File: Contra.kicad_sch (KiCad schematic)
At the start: 99 parts, among them J1 Conn_01x04, SW1 SW_PUSH, U1 ProMicro

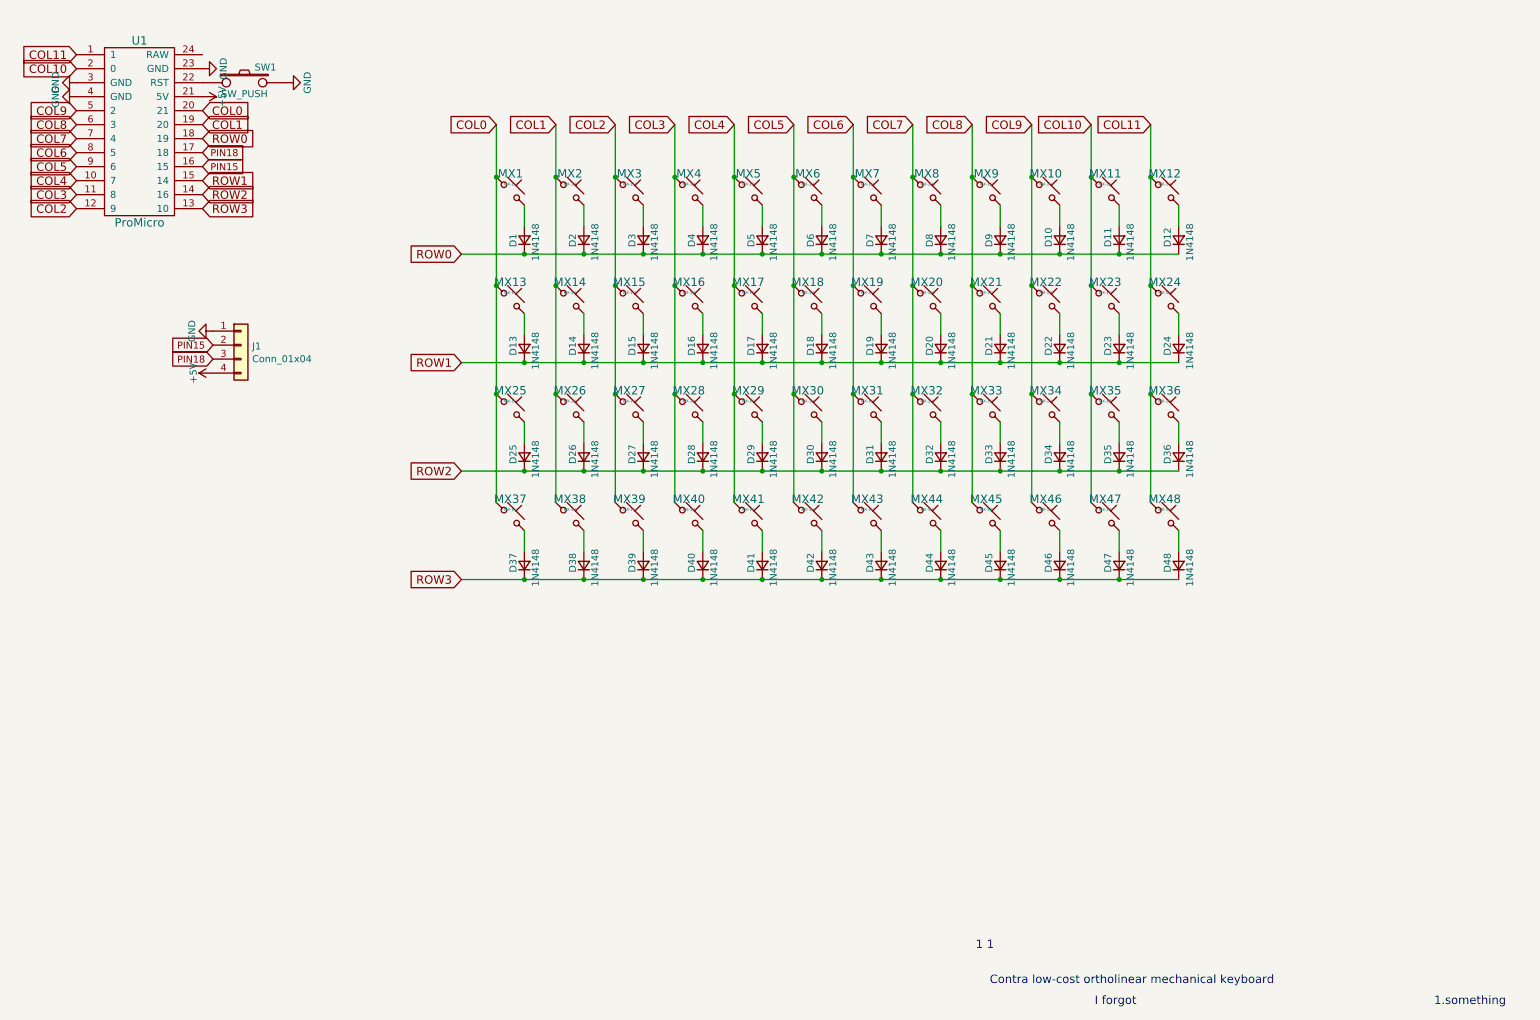
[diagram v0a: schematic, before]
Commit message: use smd diodes and palce on bottem select ks27 only footprint
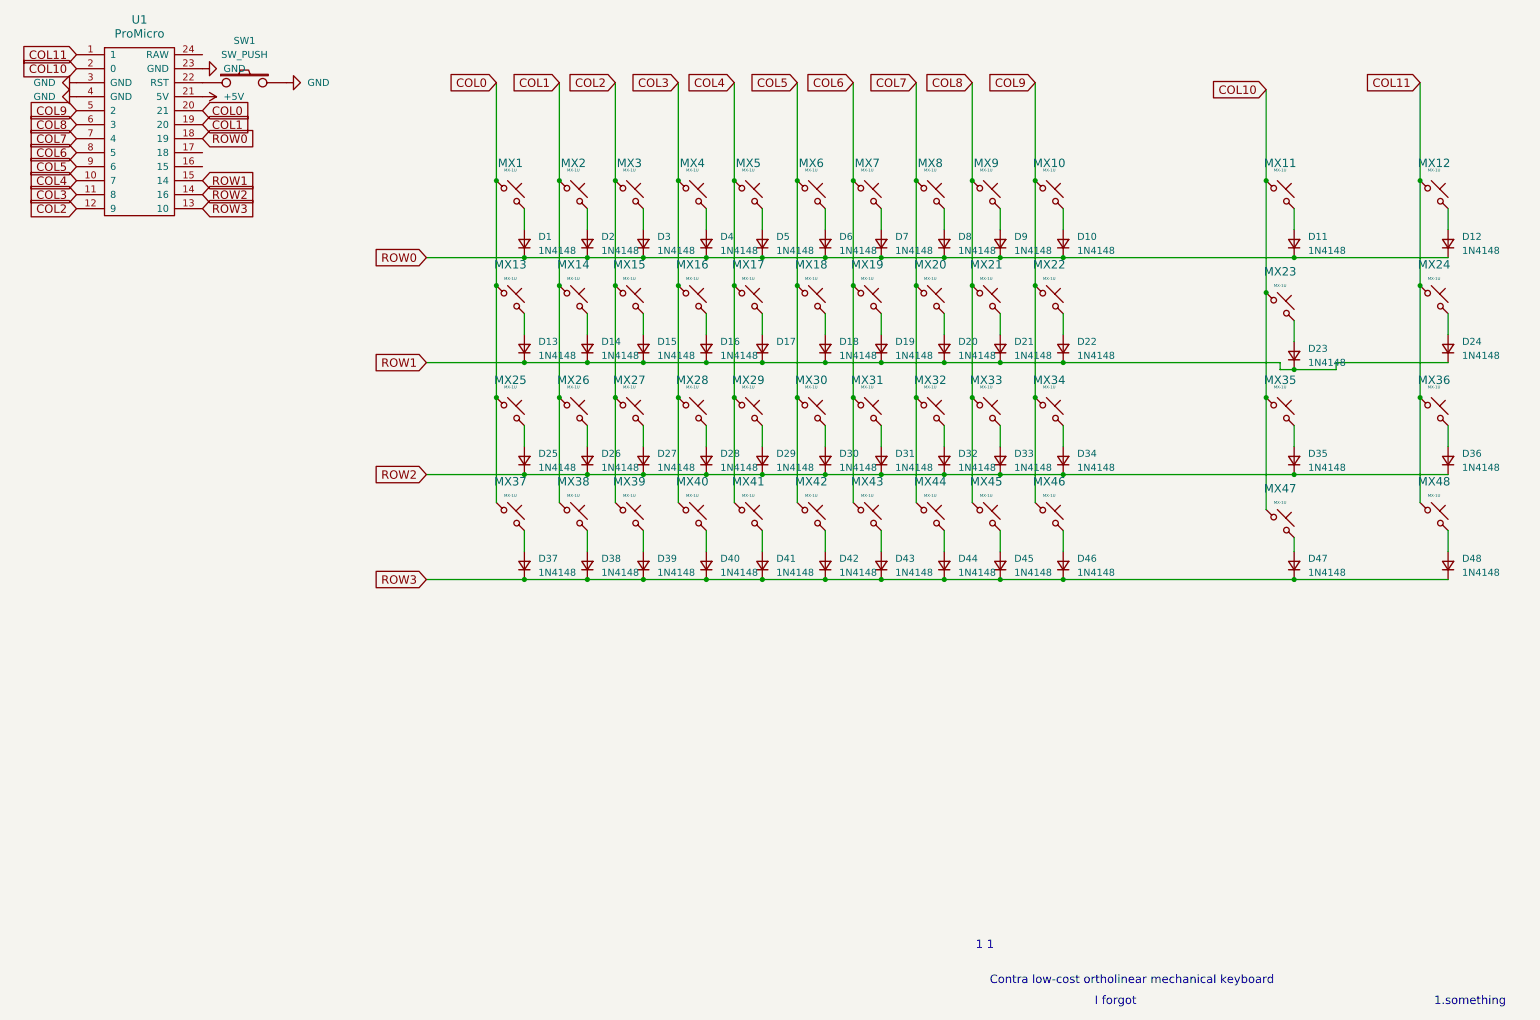
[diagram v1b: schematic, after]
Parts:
- removed J1: Conn_01x04, Pin_Headers:Pin_Header_Straight_1x04_Pitch2.54mm, symbol Connector_Generic:Conn_01x04
- D1, D10, D11, D12, D13, D14, D15, D16, D17, D18, D19, D2, D20, D21, D22, D23, D24, D25, D26, D27, D28, D29, D3, D30, D31, D32, D33, D34, D35, D36, D37, D38, D39, D4, D40, D41, D42, D43, D44, D45, D46, D47, D48, D5, D6, D7, D8, D9: footprint locallib:D_DO-35_SOD27_P7.62mm_Horizontal-DoubleSided -> Diode_SMD:D_0805_2012Metric_Pad1.15x1.40mm_HandSolder
- MX1, MX10, MX11, MX12, MX13, MX14, MX15, MX16, MX17, MX18, MX19, MX2, MX20, MX21, MX22, MX23, MX24, MX25, MX26, MX27, MX28, MX29, MX3, MX30, MX31, MX32, MX33, MX34, MX35, MX36, MX37, MX38, MX39, MX4, MX40, MX41, MX42, MX43, MX44, MX45, MX46, MX47, MX48, MX5, MX6, MX7, MX8, MX9: footprint MX_Alps_Hybrid:MX-1U-NoLED -> WLPlanckFootprints:SW_Gateron_LowProfile_HotSwap
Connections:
- net PIN15: no longer names the net of U1.16 (15)
- net PIN18: no longer names the net of U1.17 (18)
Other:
- moved on the sheet: D1, D10, D11, D12, D14, D16, D18, D2, D20, D22, D23, D24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
